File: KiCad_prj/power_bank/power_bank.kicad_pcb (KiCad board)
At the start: 2 copper layers, 70 parts, among them J1 svorkovnice, J2 svorkovnice, J3 vypinac, J4 vypinac, Q1 BC847BS, Q2 BC857BS, Q3 IRFR5305, Q4 IRFR4105, U1 LMR51625, U2 TPS564242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

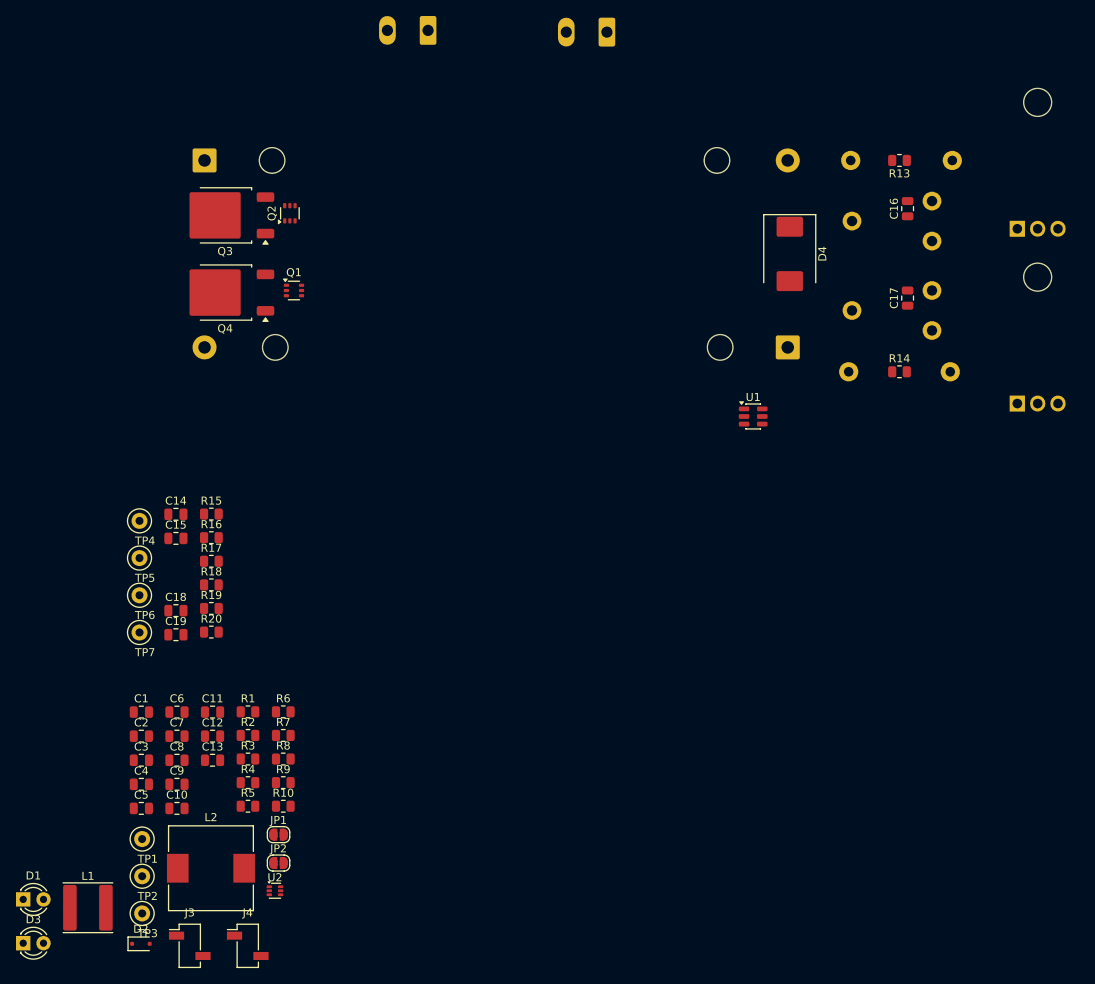
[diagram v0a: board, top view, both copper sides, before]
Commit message: power_bank: priprava pouzdra chladice
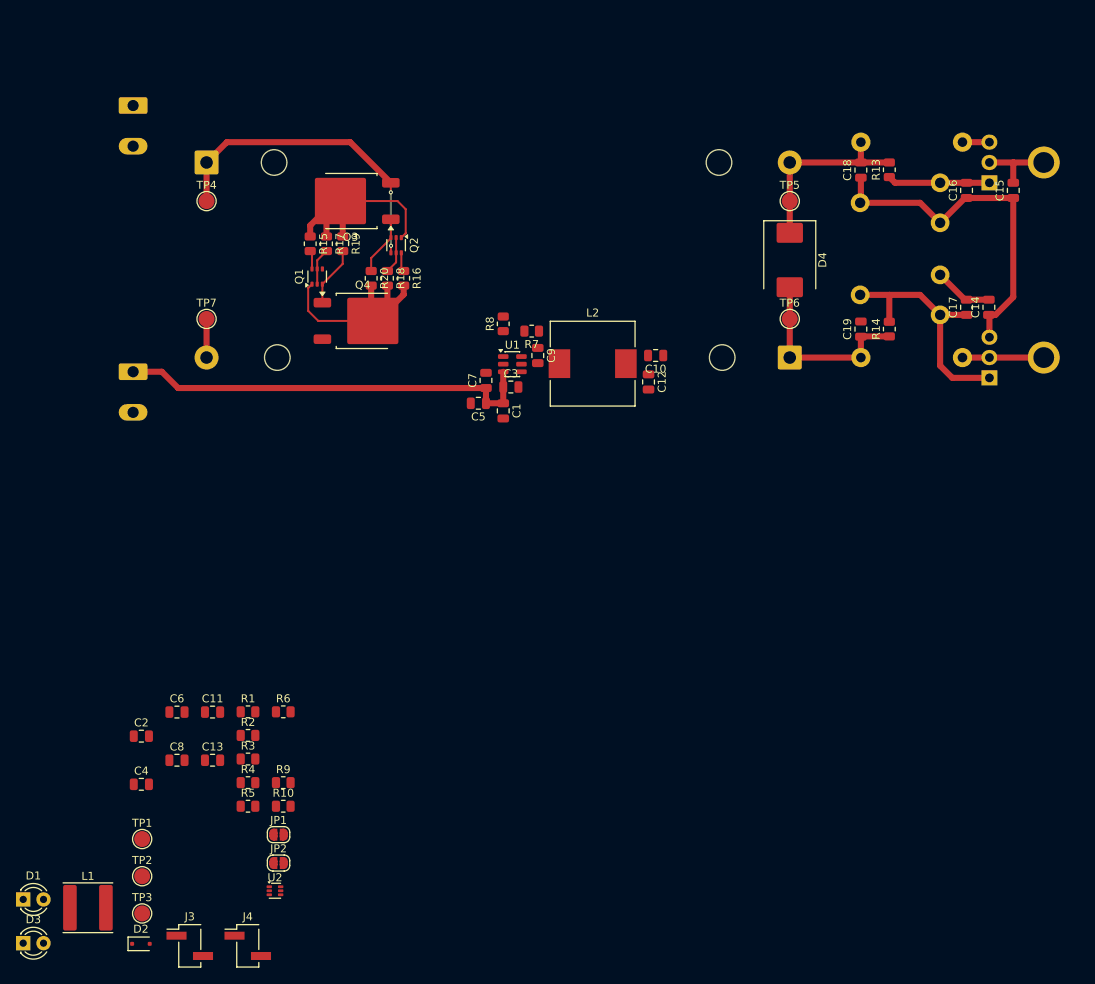
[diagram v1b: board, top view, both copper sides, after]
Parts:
- added HS1: V7142A, heatsink:V7142A, B.Cu at (208.4, 54.6)
- added HS2: V7142A, heatsink:V7142A, B.Cu at (208.4, 79.0)
- J3, J4: footprint Connector_PinSocket_2.54mm:PinSocket_1x02_P2.54mm_Vertical_SMD_Pin1Left -> Connector_PinHeader_2.54mm:PinHeader_1x02_P2.54mm_Vertical_SMD_Pin1Left
- TP1, TP2, TP3, TP4, TP5, TP6, TP7: footprint TestPoint:TestPoint_Loop_D1.80mm_Drill1.0mm_Beaded -> TestPoint:TestPoint_Pad_D2.0mm
- U3, U4: footprint Package_TO_SOT_THT:TO-220F-3_Horizontal_TabUp -> Package_TO_SOT_THT:TO-220-3_Vertical
- moved C15 113.3 mm to (206.8, 58.1), turned to 90 degrees
- moved C14 104.9 mm to (203.7, 72.7), turned to 90 degrees
- moved C18 101.8 mm to (187.7, 55.6), turned to 90 degrees
- moved C19 93.8 mm to (187.7, 75.4), turned to 90 degrees
- moved TP5 92.7 mm to (178.8, 59.4)
- moved TP6 88.3 mm to (178.8, 74.2)
- moved C10 82.4 mm to (162.1, 78.7), turned to 180 degrees
- moved L2 79.1 mm to (154.2, 79.8)
- moved J1 72.9 mm to (96.7, 80.8), turned to -90 degrees
- moved C12 70.2 mm to (161.2, 82.0), turned to -90 degrees
- moved C9 70.1 mm to (147.3, 78.7), turned to -90 degrees
- moved C5 65.9 mm to (139.9, 84.7), turned to 180 degrees
- moved C3 65.6 mm to (144.0, 82.7)
- moved R8 61.0 mm to (143.0, 74.8), turned to 90 degrees
- moved R7 59.3 mm to (146.6, 75.7), turned to 180 degrees
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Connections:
- Q4 pad 2: GND -> /VIN_GND
- Q4 pad 3: /VIN_GND -> GND
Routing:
- net /Battery/CHA_POS: track 0.00 -> 72.3 mm
- net /VIN_from_+20V_to_+50V: track 0.00 -> 53.0 mm
- net /VIN_GND: track 0.00 -> 44.9 mm
- net /Battery/BAT_POS: track 0.00 -> 39.8 mm, vias 0 -> 2
- net Net-(U4-ADJ): track 0.00 -> 30.8 mm
- net Net-(BT2-+): track 0.00 -> 23.9 mm
- net Net-(BT1--): track 0.00 -> 23.8 mm
- net Net-(U3-ADJ): track 0.00 -> 12.8 mm
- net Net-(U4-VO): track 0.00 -> 10.2 mm
- net Net-(Q1B-C2): track 0.00 -> 7.51 mm
- net Net-(Q2B-C2): track 0.00 -> 7.49 mm
- net GND: track 0.00 -> 4.83 mm
- net Net-(Q2A-B1): track 0.00 -> 4.62 mm
- net Net-(Q1A-B1): track 0.00 -> 4.62 mm
- net Net-(U3-VO): track 0.00 -> 3.37 mm
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
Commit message: power_bank: zakladni vzhled DPS
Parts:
- added C20: 330n, Capacitor_SMD:C_0805_2012Metric, F.Cu at (126.8, 90.4)
- D1, D3: moved to B.Cu
- J3, J4: footprint Connector_PinHeader_2.54mm:PinHeader_1x02_P2.54mm_Vertical_SMD_Pin1Left -> Connector_PinHeader_2.54mm:PinHeader_1x02_P2.54mm_Vertical; moved to B.Cu
- moved D1 128.8 mm to (191.8, 77.7), turned to 180 degrees
- moved D3 114.2 mm to (191.6, 117.0), turned to 180 degrees
- moved J4 102.8 mm to (181.6, 77.7), turned to -90 degrees
- moved JP2 92.1 mm to (182.9, 80.0), turned to 180 degrees
- moved J3 85.5 mm to (181.6, 117.0), turned to -90 degrees
- moved L1 78.1 mm to (131.6, 81.0), turned to -90 degrees
- moved TP3 77.9 mm to (157.0, 97.8)
- moved JP1 72.0 mm to (182.9, 114.8)
- moved TP2 66.8 mm to (146.3, 97.8)
- moved U2 63.0 mm to (126.7, 83.8), turned to 180 degrees
- moved TP1 60.7 mm to (99.8, 78.5)
- moved C4 58.5 mm to (124.7, 80.5), turned to -90 degrees
- moved R9 57.5 mm to (136.7, 78.6), turned to -90 degrees
- moved C2 55.6 mm to (123.8, 77.2), turned to 180 degrees
- moved C8 51.7 mm to (119.0, 80.5), turned to -90 degrees
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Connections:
- D1 pad 1: Net-(D1-K) -> GND
- D1 pad 2: /VOUT_+5V -> Net-(D1-A)
- D2 pad 1: /VIN_from_+20V_to_+50V -> Net-(D2-K)
- D2 pad 2: Net-(D2-A) -> /EN_IN
- D3 pad 1: Net-(D3-K) -> /VIN_GND
- D3 pad 2: /Battery/CHA_POS -> Net-(D3-A)
- J3 pad 1: Net-(J3-Pin_1) -> /VIN_from_+20V_to_+50V
- J3 pad 2: /EN_IN -> Net-(J3-Pin_2)
- JP1 pad 1: Net-(J3-Pin_1) -> /VIN_from_+20V_to_+50V
- JP1 pad 2: /EN_IN -> Net-(J3-Pin_2)
- R1 pad 1: GND -> Net-(D1-A)
- R1 pad 2: Net-(D1-K) -> /VOUT_+5V
- R10 pad 1: /VIN_GND -> Net-(D3-A)
- R10 pad 2: Net-(D3-K) -> /Battery/CHA_POS
- R4 pad 1: Net-(D2-A) -> Net-(J3-Pin_2)
- R4 pad 2: Net-(J3-Pin_1) -> Net-(D2-K)
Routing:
- net /Battery/CHA_POS: track 72.3 -> 168.3 mm
- net /EN_OUT: track 0.00 -> 76.7 mm, vias 0 -> 2
- net Net-(D1-A): track 0.00 -> 74.9 mm
- net Net-(J3-Pin_2): track 0.00 -> 57.0 mm
- net /VIN_from_+20V_to_+50V: track 53.0 -> 101.1 mm
- net Net-(J4-Pin_1): track 0.00 -> 47.5 mm
- net /VOUT_+5V: track 0.00 -> 44.9 mm
- net Net-(D3-A): track 0.00 -> 32.1 mm
- net /Battery/BAT_POS: track 39.8 -> 64.2 mm
- net GND: track 4.83 -> 16.5 mm, vias 0 -> 13
- net /FB_OUT: track 0.00 -> 11.5 mm
- net /EN_IN: track 0.00 -> 8.18 mm
- net /FB_IN: track 0.00 -> 5.97 mm
- net /SWN_IN: track 0.00 -> 4.83 mm
- net /SWN_OUT: track 0.00 -> 4.49 mm
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- added copper zone on B.Cu, net /VIN_GND
- added copper zone on B.Cu, net GND
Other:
- board outline added: 130 x 60 mm

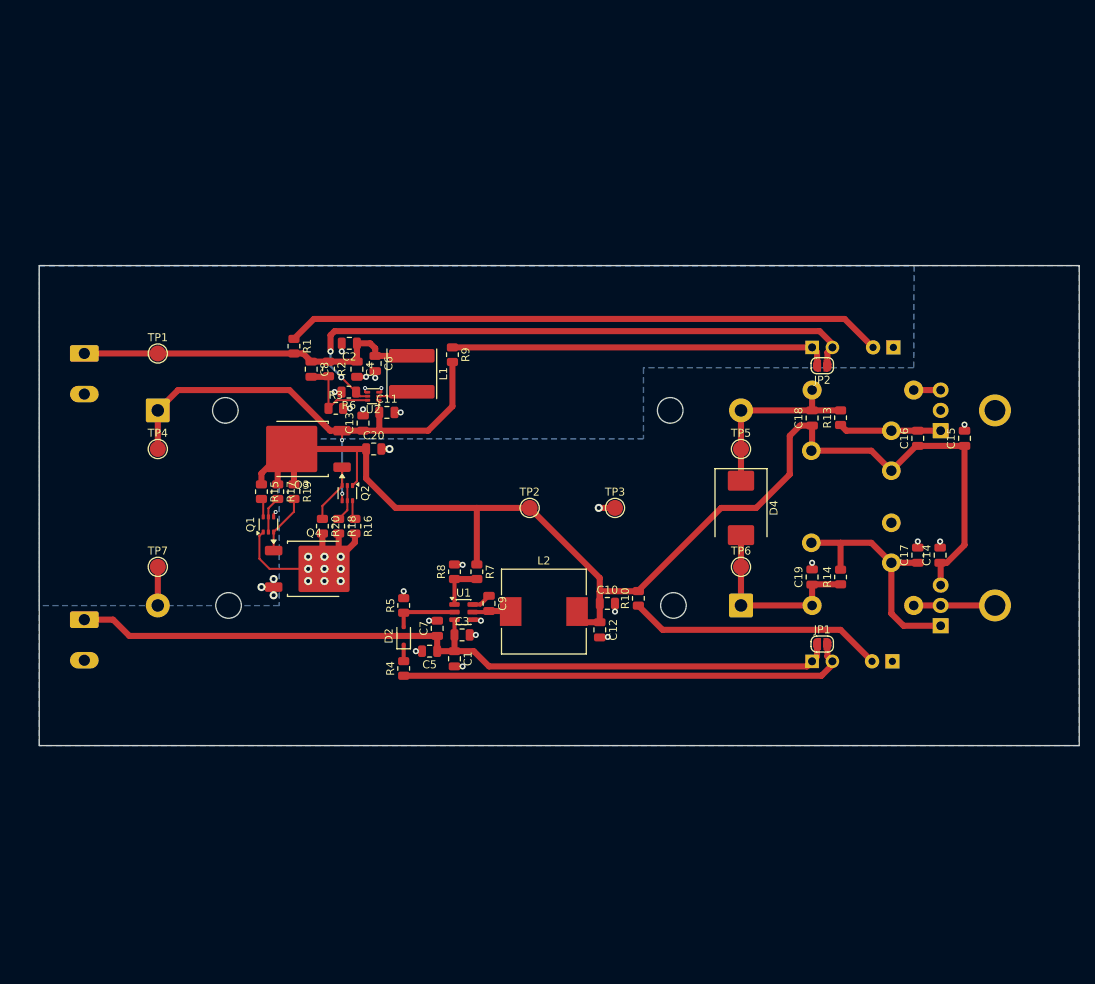
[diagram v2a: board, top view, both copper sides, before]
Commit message: power_bank: vyrobni rozmisteni prvku, doplnit uzivatelske popisky
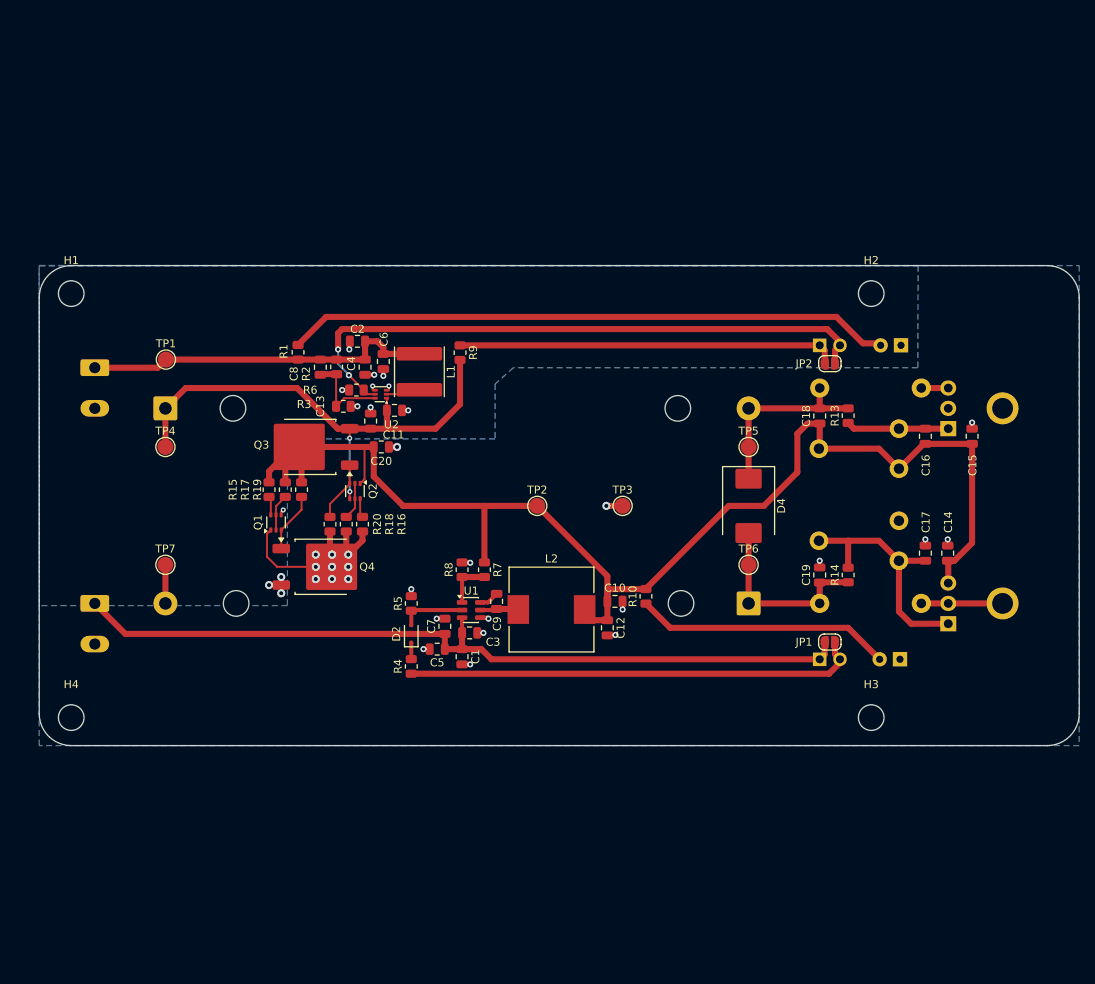
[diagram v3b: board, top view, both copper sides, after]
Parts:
- added H1: M3, MountingHole:MountingHole_3.2mm_M3, F.Cu at (89.0, 71.0)
- added H2: M3, MountingHole:MountingHole_3.2mm_M3, F.Cu at (189.0, 71.0)
- added H3: M3, MountingHole:MountingHole_3.2mm_M3, F.Cu at (189.0, 124.0)
- added H4: M3, MountingHole:MountingHole_3.2mm_M3, F.Cu at (89.0, 124.0)
- moved J1 2.41 mm to (91.9, 109.7)
- moved J2 2.21 mm to (91.9, 80.3)
- moved TP1 1.27 mm to (100.8, 79.2)
- moved C8 1.17 mm to (120.1, 80.2)
- moved C4 1.05 mm to (125.7, 80.2)
- moved R2 1.05 mm to (122.2, 80.2)
- moved C2 1.05 mm to (124.8, 77.0)
- moved C6 1.05 mm to (128.0, 79.5)
- moved C3 0.98 mm to (138.8, 113.4)
- moved C5 0.98 mm to (134.7, 115.4)
- moved J3 0.98 mm to (182.6, 116.7)
- moved JP2 0.98 mm to (183.8, 79.8)
- moved L2 0.98 mm to (149.0, 110.5)
- moved R14 0.98 mm to (186.1, 106.2)
- moved R7 0.98 mm to (140.7, 105.5)
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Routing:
- net Net-(D1-A): track 74.9 -> 75.8 mm
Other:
- outline, holes or cut-outs redrawn

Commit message: power_bank: dokoncena DPS
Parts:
- added G***: LOGO, images:battery, B.Cu at (143.8, 71.1)
- added G***: LOGO, images:battery, B.Cu at (143.8, 124.0)
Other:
- board text added: "${TITLE}"
- board text added: "+12V<>VIN-GND"
- board text added: "+5V<>GND"
- board text added: "+V_{BAT}<>GND"
- board text added: "+V_{BT2}<>VIN-GND"
- board text added: "-V_{BT1}<>+12V"
- board text added: "10W"
- board text added: "20V-55V"
- board text added: "GND"
- board text added: "INPUT -V|+V"
- board text added: "INPUT Active"
- board text added: "ON/OFF Input"
- board text added: "ON/OFF Output"
- board text added: "OUTPUT Active"
- board text added: "OUTPUT GND|+5V"
- board text added: "VIN-GND"
- board text added: "rev. ${REVISION}"

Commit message: Odeslano do vyroby, rev 1.0
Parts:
- added C21: 220n, Capacitor_SMD:C_0805_2012Metric, F.Cu at (133.6, 112.6)
- C1, C3, C5, C7: value 330n -> 220n
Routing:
- net /VIN_GND: track 42.9 -> 45.0 mm, vias 24 -> 25
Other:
- board text added: "20V-50V"
- board text removed: "20V-55V"
